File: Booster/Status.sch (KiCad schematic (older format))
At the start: 37 parts

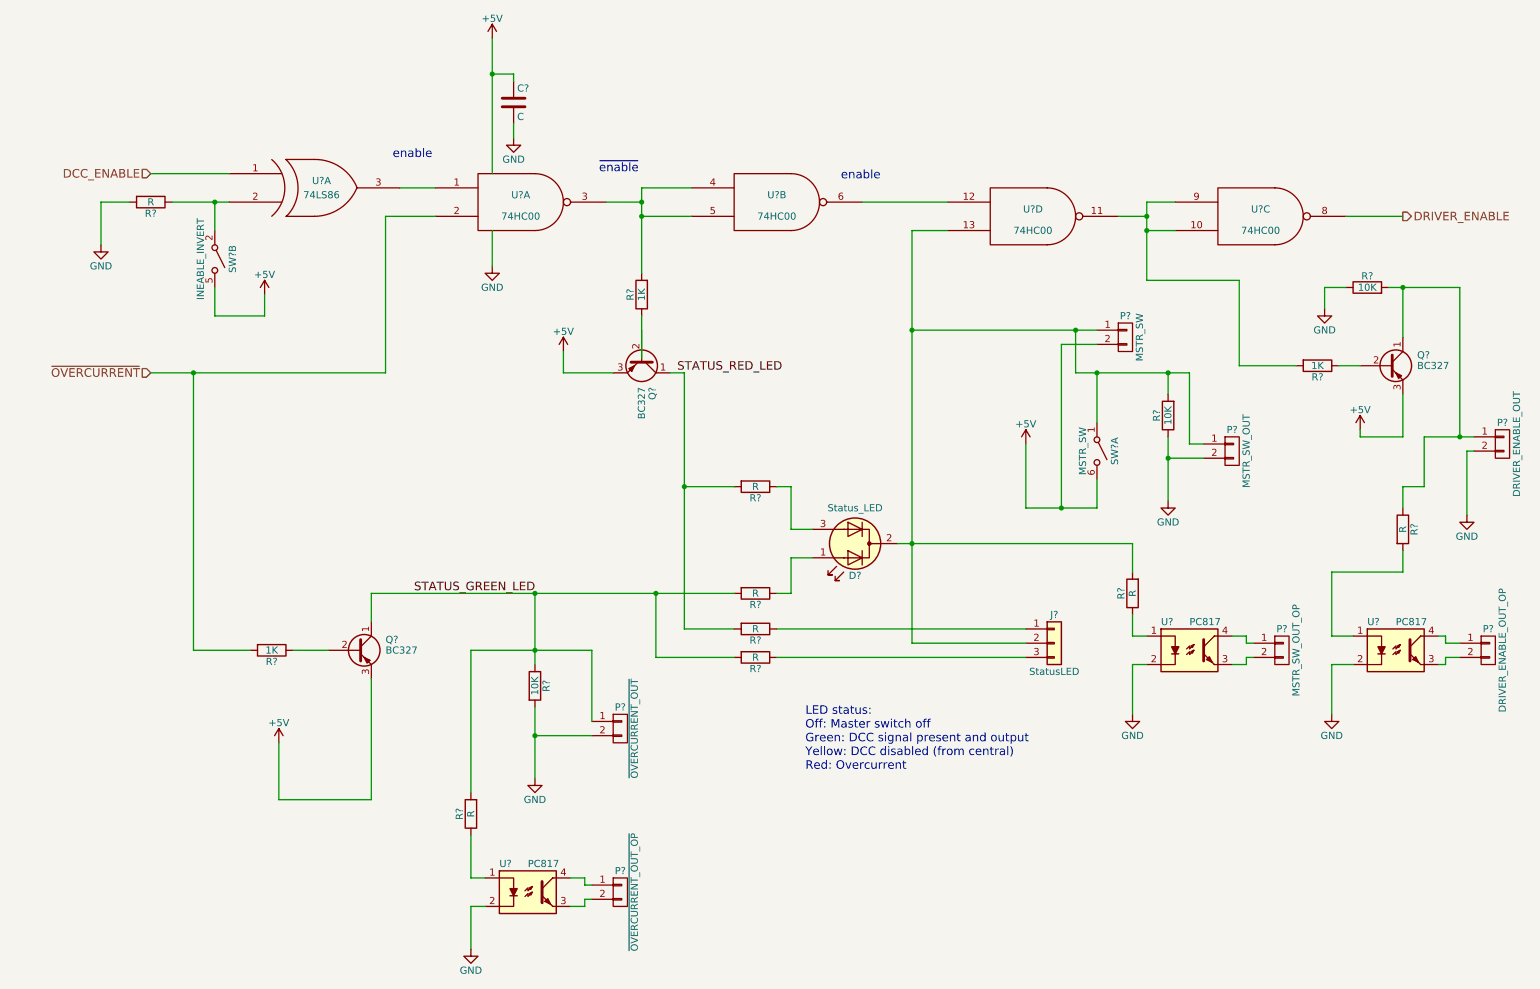
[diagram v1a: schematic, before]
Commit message: Kind of working with the overcurrent retry, but not liking the RC delay in the final output to the motor driver.
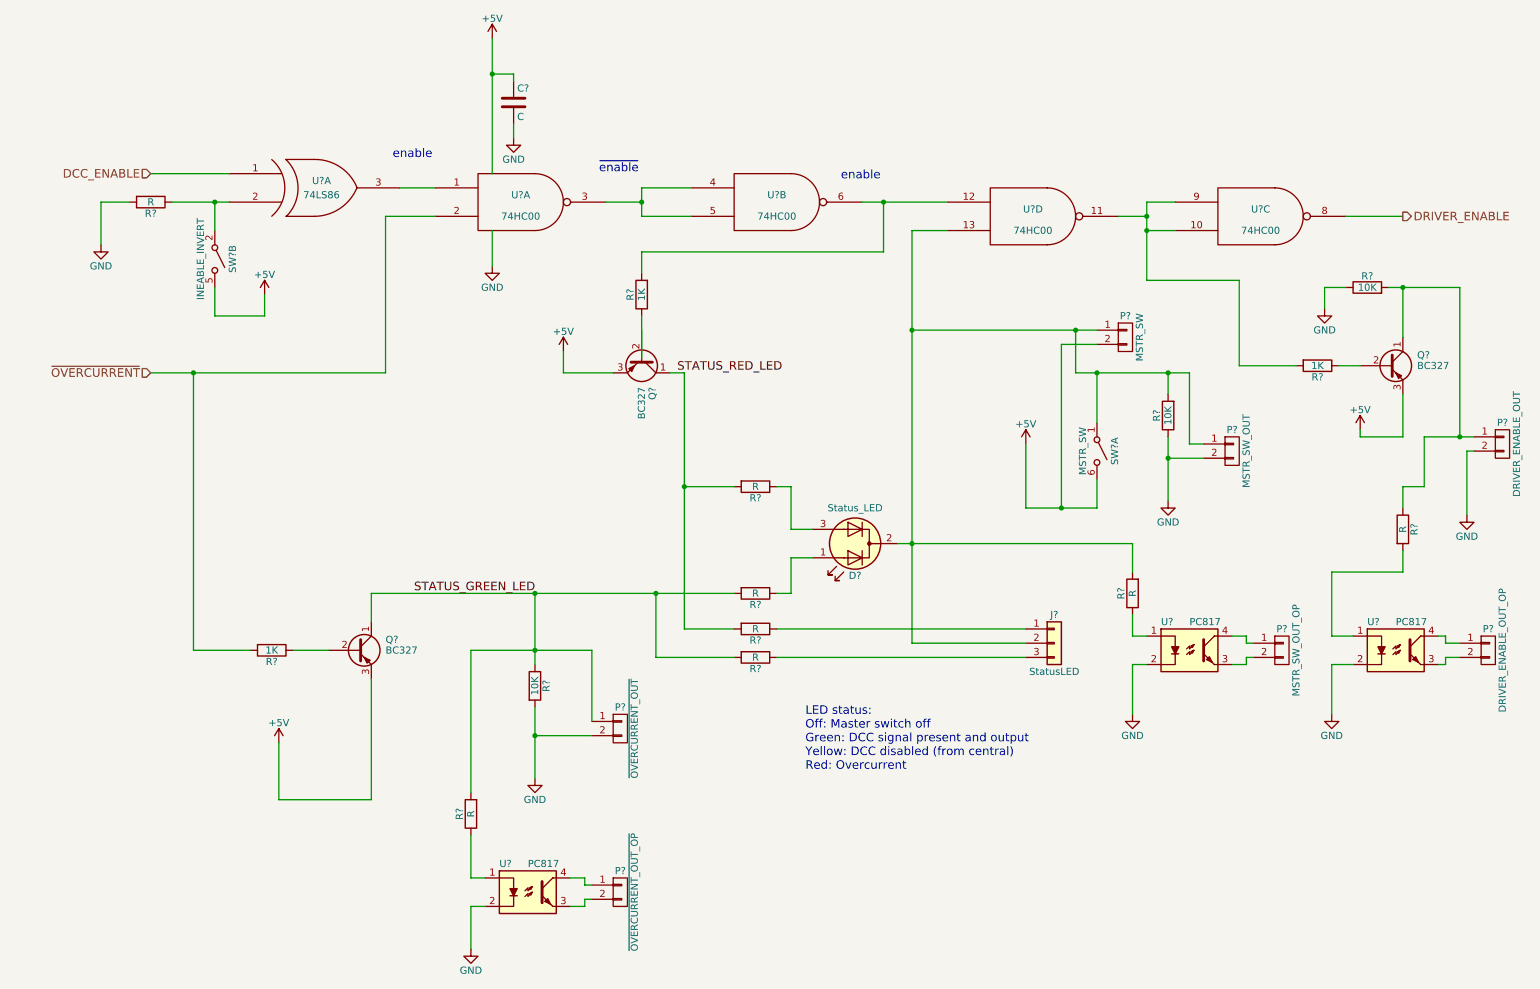
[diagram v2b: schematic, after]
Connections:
- net at U?.3, U?.4, U?.5: no longer R?.2
- net at U?.12, U?.6: now also R?.2
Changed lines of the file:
@@
 $EndComp
 Wire Wire Line
-	1450 3150 1750 3150
-Wire Wire Line
-	1750 3150 3100 3150
+	1450 3150 3100 3150
 Wire Wire Line
 	1450 1750 2000 1750
@@
 	6800 2150 7050 2150
 Wire Wire Line
-	6800 2150 6800 2850
-Wire Wire Line
-	6800 2850 6800 4350
-Wire Wire Line
-	6800 4350 6800 5050
+	6800 2150 6800 5050
 Wire Wire Line
 	7600 4100 7600 3650
@@
 Connection ~ 6800 2850
 Wire Wire Line
-	7600 4100 7850 4100
-Wire Wire Line
-	7850 4100 8100 4100
+	7600 4100 8100 4100
 Wire Wire Line
 	8100 4100 8100 3900
 Wire Wire Line
-	7950 3150 8100 3150
-Wire Wire Line
-	8100 3150 8600 3150
-Wire Wire Line
-	8600 3150 8750 3150
+	7950 3150 8750 3150
 Wire Wire Line
 	7950 3150 7950 2850
@@
 	3000 4900 3000 4700
 Wire Wire Line
-	3000 4700 4150 4700
-Wire Wire Line
-	4150 4700 5000 4700
-Wire Wire Line
-	5000 4700 5550 4700
+	3000 4700 5550 4700
 Wire Wire Line
 	6100 4250 5950 4250
@@
 	5950 4450 6100 4450
 Wire Wire Line
-	5200 3150 5200 3950
-Wire Wire Line
-	5200 3950 5200 4950
+	5200 3150 5200 4950
 Wire Wire Line
 	5200 4950 5550 4950
@@
 Connection ~ 5000 4700
 Wire Wire Line
-	6700 4350 6800 4350
-Wire Wire Line
-	6800 4350 8350 4350
+	6700 4350 8350 4350
 Wire Wire Line
 	6800 5050 7600 5050
@@
 	7850 2950 7850 4100
 Wire Wire Line
-	6800 2850 7950 2850
-Wire Wire Line
-	7950 2850 8100 2850
+	6800 2850 8100 2850
 Connection ~ 7850 4100
 Wire Wire Line
@@
 	10250 2900 10250 2550
 Wire Wire Line
-	10150 2550 10250 2550
-Wire Wire Line
-	10250 2550 10650 2550
+	10150 2550 10650 2550
 Wire Wire Line
 	10650 2550 10650 3600
 Wire Wire Line
-	10400 3600 10650 3600
-Wire Wire Line
-	10650 3600 10750 3600
+	10400 3600 10750 3600
 Wire Wire Line
 	10250 3600 9950 3600
@@
 	9700 2550 9700 2700
 Wire Wire Line
-	4150 4700 4150 5100
-Wire Wire Line
-	4150 5100 4150 5200
+	4150 4700 4150 5200
 Connection ~ 4150 4700
 Wire Wire Line
-	4150 5500 4150 5700
-Wire Wire Line
-	4150 5700 4150 6000
-Wire Wire Line
-	8600 3600 8600 3750
-Wire Wire Line
-	8600 3750 8600 4050
+	4150 5500 4150 6000
+Wire Wire Line
+	8600 3600 8600 4050
 Wire Wire Line
 	8600 3150 8600 3300
@@
 	4550 5100 4550 5600
 Wire Wire Line
-	3700 5100 4150 5100
-Wire Wire Line
-	4150 5100 4550 5100
+	3700 5100 4550 5100
 Connection ~ 4150 5100
 Wire Wire Line
@@
 	4650 1950 4900 1950
 Wire Wire Line
-	4900 1850 4900 1950
-Wire Wire Line
-	4900 1950 4900 2050
-Wire Wire Line
-	4900 2050 4900 2450
-Wire Wire Line
 	4900 1850 5250 1850
 Wire Wire Line
@@
 	8250 2050 8450 2050
 Wire Wire Line
-	8450 1950 8450 2050
-Wire Wire Line
-	8450 2050 8450 2150
-Wire Wire Line
-	8450 2150 8450 2500
+	8450 1950 8450 2500
 Wire Wire Line
 	8450 1950 8650 1950
@@
 Wire Wire Line
 	6450 1950 7050 1950
-Connection ~ 4900 2050
 Wire Wire Line
 	4900 3050 4900 2750
@@
 	9850 2050 10250 2050
 Wire Wire Line
-	1600 1950 1900 1950
-Wire Wire Line
-	1900 1950 2000 1950
+	1600 1950 2000 1950
 Wire Wire Line
 	1300 1950 1100 1950
@@
 	3850 2150 3850 2400
 Wire Wire Line
-	3850 800  3850 1050
-Wire Wire Line
-	3850 1050 3850 1750
+	3850 800  3850 1750
 Wire Wire Line
 	3850 1050 4000 1050
@@
 Wire Wire Line
 	4000 1400 4000 1500
+Wire Wire Line
+	4900 1850 4900 2050
+Wire Wire Line
+	4900 2450 4900 2300
+Wire Wire Line
+	4900 2300 6600 2300
+Wire Wire Line
+	6600 2300 6600 1950
+Connection ~ 6600 1950
 $EndSCHEMATC

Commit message: Added 555 timer to control overcurrent release delay. Simpler to control as turning the power off cleared the overflow before the capacitor controlling the release delay was fully cleared. The LM339 is still doing the detect delay.
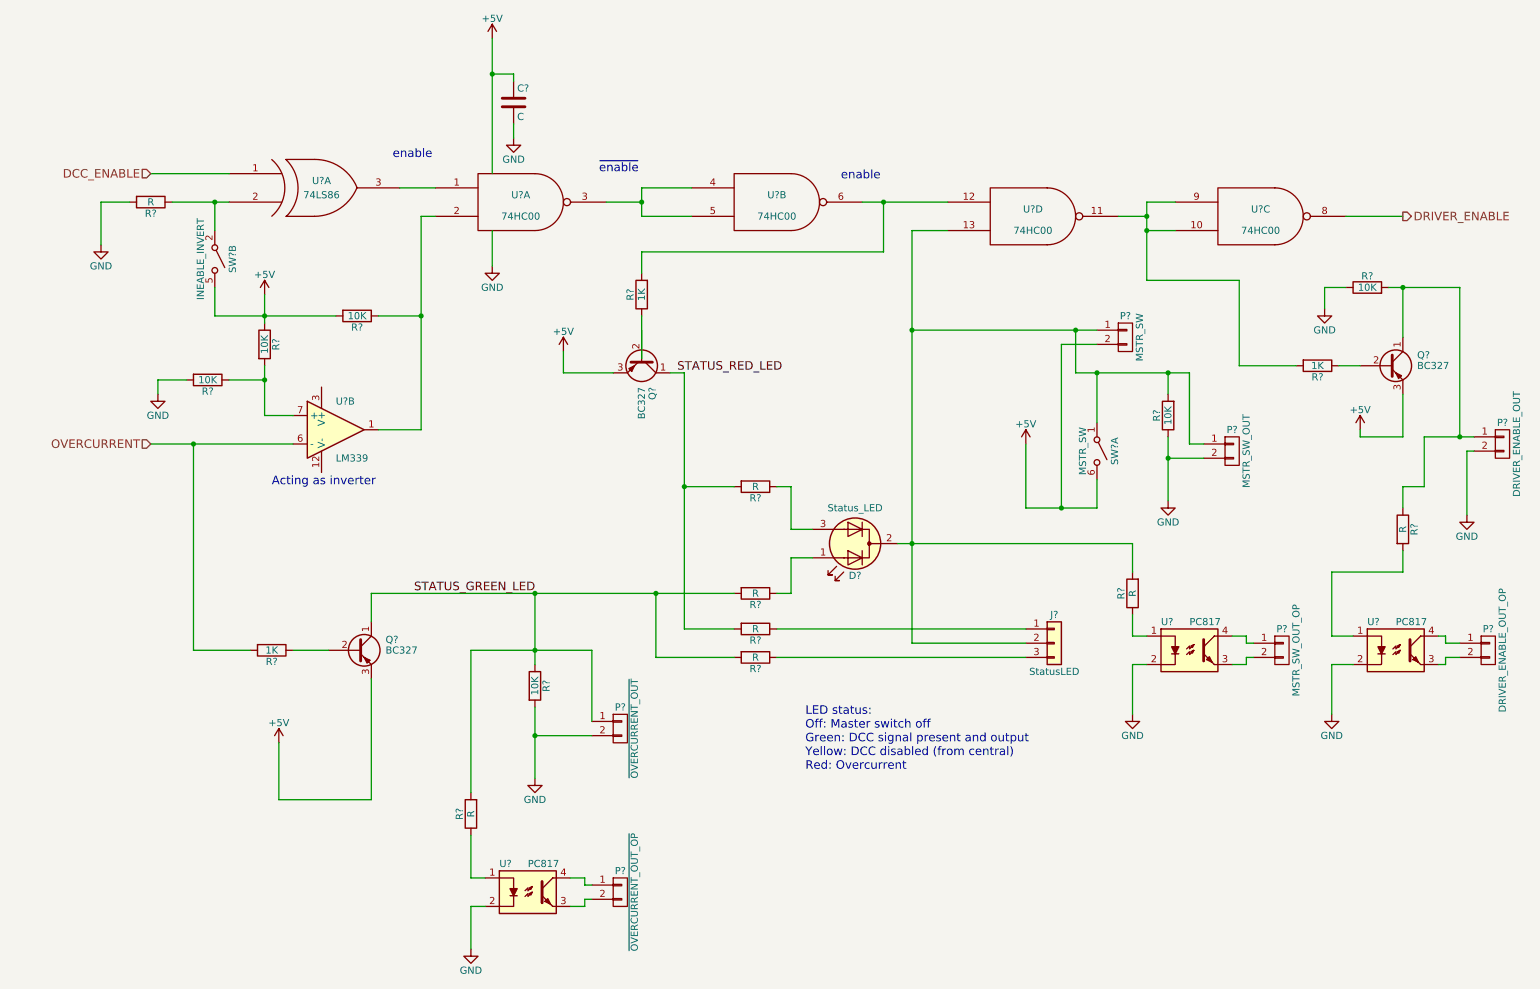
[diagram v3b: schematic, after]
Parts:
- added R? (x3): 10K, symbol R
- added U?: LM339, symbol LM339
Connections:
- net +5V: now also R?.1, R?.2
- net GND: now also R?.2
- net ~OVERCURRENT: no longer names the net of U?.2
- net ~OVERCURRENT: now also R?.1, U?.1; no longer R?.2
- new net: R?.1, R?.2, U?.7 (+)
- new net OVERCURRENT: R?.2, U?.6 (-)
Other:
- note added: "Acting as inverter"
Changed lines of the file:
@@
 Text HLabel 1450 1750 0    60   Input ~ 0
 DCC_ENABLE
-Text HLabel 1450 3150 0    60   Input ~ 0
-~OVERCURRENT
+Text HLabel 1450 3650 0    60   Input ~ 0
+OVERCURRENT
 Text HLabel 10250 2050 2    60   Output ~ 0
 DRIVER_ENABLE
@@
 $EndComp
 Wire Wire Line
-	1450 3150 3100 3150
-Wire Wire Line
 	1450 1750 2000 1750
 Wire Wire Line
-	1750 3150 1750 5100
+	1750 3650 1750 5100
 Wire Wire Line
 	6800 2150 7050 2150
 Wire Wire Line
-	6800 2150 6800 5050
+	6800 2150 6800 2850
+Wire Wire Line
+	6800 2850 6800 4350
+Wire Wire Line
+	6800 4350 6800 5050
 Wire Wire Line
 	7600 4100 7600 3650
@@
 Connection ~ 6800 2850
 Wire Wire Line
-	7600 4100 8100 4100
+	7600 4100 7850 4100
+Wire Wire Line
+	7850 4100 8100 4100
 Wire Wire Line
 	8100 4100 8100 3900
 Wire Wire Line
-	7950 3150 8750 3150
+	7950 3150 8100 3150
+Wire Wire Line
+	8100 3150 8600 3150
+Wire Wire Line
+	8600 3150 8750 3150
 Wire Wire Line
 	7950 3150 7950 2850
@@
 Wire Wire Line
 	1750 5100 2150 5100
-Connection ~ 1750 3150
+Connection ~ 1750 3650
 Wire Wire Line
 	2450 5100 2700 5100
@@
 	3000 4900 3000 4700
 Wire Wire Line
-	3000 4700 5550 4700
+	3000 4700 4150 4700
+Wire Wire Line
+	4150 4700 5000 4700
+Wire Wire Line
+	5000 4700 5550 4700
 Wire Wire Line
 	6100 4250 5950 4250
@@
 	5950 4450 6100 4450
 Wire Wire Line
-	5200 3150 5200 4950
+	5200 3150 5200 3950
+Wire Wire Line
+	5200 3950 5200 4950
 Wire Wire Line
 	5200 4950 5550 4950
@@
 Connection ~ 5000 4700
 Wire Wire Line
-	6700 4350 8350 4350
+	6700 4350 6800 4350
+Wire Wire Line
+	6800 4350 8350 4350
 Wire Wire Line
 	6800 5050 7600 5050
@@
 	7850 2950 7850 4100
 Wire Wire Line
-	6800 2850 8100 2850
+	6800 2850 7950 2850
+Wire Wire Line
+	7950 2850 8100 2850
 Connection ~ 7850 4100
 Wire Wire Line
@@
 	10250 2900 10250 2550
 Wire Wire Line
-	10150 2550 10650 2550
+	10150 2550 10250 2550
+Wire Wire Line
+	10250 2550 10650 2550
 Wire Wire Line
 	10650 2550 10650 3600
 Wire Wire Line
-	10400 3600 10750 3600
+	10400 3600 10650 3600
+Wire Wire Line
+	10650 3600 10750 3600
 Wire Wire Line
 	10250 3600 9950 3600
@@
 	9700 2550 9700 2700
 Wire Wire Line
-	4150 4700 4150 5200
+	4150 4700 4150 5100
+Wire Wire Line
+	4150 5100 4150 5200
 Connection ~ 4150 4700
 Wire Wire Line
-	4150 5500 4150 6000
-Wire Wire Line
-	8600 3600 8600 4050
+	4150 5500 4150 5700
+Wire Wire Line
+	4150 5700 4150 6000
+Wire Wire Line
+	8600 3600 8600 3750
+Wire Wire Line
+	8600 3750 8600 4050
 Wire Wire Line
 	8600 3150 8600 3300
@@
 	4550 5100 4550 5600
 Wire Wire Line
-	3700 5100 4550 5100
+	3700 5100 4150 5100
+Wire Wire Line
+	4150 5100 4550 5100
 Connection ~ 4150 5100
 Wire Wire Line
@@
 	3700 6900 3700 7200
 Wire Wire Line
-	3100 3150 3100 2050
-Wire Wire Line
-	3100 2050 3450 2050
+	3350 2050 3350 2750
+Wire Wire Line
+	3350 2750 3350 3550
+Wire Wire Line
+	3350 2050 3450 2050
 Wire Wire Line
 	3200 1850 3450 1850
@@
 	8250 2050 8450 2050
 Wire Wire Line
-	8450 1950 8450 2500
+	8450 1950 8450 2050
+Wire Wire Line
+	8450 2050 8450 2150
+Wire Wire Line
+	8450 2150 8450 2500
 Wire Wire Line
 	8450 1950 8650 1950
@@
 Connection ~ 8450 2150
 Wire Wire Line
-	6450 1950 7050 1950
+	6450 1950 6600 1950
+Wire Wire Line
+	6600 1950 7050 1950
 Wire Wire Line
 	4900 3050 4900 2750
@@
 	9850 2050 10250 2050
 Wire Wire Line
-	1600 1950 2000 1950
+	1600 1950 1900 1950
+Wire Wire Line
+	1900 1950 2000 1950
 Wire Wire Line
 	1300 1950 1100 1950
@@
 	1900 2750 2250 2750
 Wire Wire Line
-	2250 2750 2250 2600
+	2250 2750 2750 2750
+Wire Wire Line
+	2250 2600 2250 2750
+Wire Wire Line
+	2250 2750 2250 2800
 Wire Wire Line
 	3850 2150 3850 2400
 Wire Wire Line
-	3850 800  3850 1750
+	3850 800  3850 1050
+Wire Wire Line
+	3850 1050 3850 1750
 Wire Wire Line
 	3850 1050 4000 1050
@@
 	4000 1400 4000 1500
 Wire Wire Line
-	4900 1850 4900 2050
+	4900 1850 4900 1950
+Wire Wire Line
+	4900 1950 4900 2050
 Wire Wire Line
 	4900 2450 4900 2300
@@
 	6600 2300 6600 1950
 Connection ~ 6600 1950
+$Comp
+L LM339 U?
+U 2 1 5A375C9A
+P 2750 3550
+F 0 "U?" H 2750 3750 50  0000 L CNN
+F 1 "LM339" H 2750 3350 50  0000 L CNN
+F 2 "" H 2700 3650 50  0000 C CNN
+F 3 "" H 2800 3750 50  0000 C CNN
+	2    2750 3550
+	1    0    0    -1
+$EndComp
+Wire Wire Line
+	1450 3650 1750 3650
+Wire Wire Line
+	1750 3650 2450 3650
+Wire Wire Line
+	2250 3450 2450 3450
+Wire Wire Line
+	2250 3100 2250 3200
+Wire Wire Line
+	2250 3200 2250 3450
+Wire Wire Line
+	2000 3200 2250 3200
+$Comp
+L R R?
+U 1 1 5A376953
+P 2250 2950
+F 0 "R?" V 2330 2950 50  0000 C CNN
+F 1 "10K" V 2250 2950 50  0000 C CNN
+F 2 "" V 2180 2950 50  0000 C CNN
+F 3 "" H 2250 2950 50  0000 C CNN
+	1    2250 2950
+	1    0    0    -1
+$EndComp
+Connection ~ 2250 3200
+Connection ~ 2250 2750
+$Comp
+L R R?
+U 1 1 5A376D88
+P 1850 3200
+F 0 "R?" V 1930 3200 50  0000 C CNN
+F 1 "10K" V 1850 3200 50  0000 C CNN
+F 2 "" V 1780 3200 50  0000 C CNN
+F 3 "" H 1850 3200 50  0000 C CNN
+	1    1850 3200
+	0    1    1    0
+$EndComp
+Wire Wire Line
+	1700 3200 1500 3200
+Wire Wire Line
+	1500 3200 1500 3300
+$Comp
+L GND #PWR?
+U 1 1 5A376ECE
+P 1500 3300
+F 0 "#PWR?" H 1500 3050 50  0001 C CNN
+F 1 "GND" H 1500 3150 50  0000 C CNN
+F 2 "" H 1500 3300 50  0000 C CNN
+F 3 "" H 1500 3300 50  0000 C CNN
+	1    1500 3300
+	1    0    0    -1
+$EndComp
+Wire Wire Line
+	3350 3550 3050 3550
+$Comp
+L R R?
+U 1 1 5A377144
+P 2900 2750
+F 0 "R?" V 2980 2750 50  0000 C CNN
+F 1 "10K" V 2900 2750 50  0000 C CNN
+F 2 "" V 2830 2750 50  0000 C CNN
+F 3 "" H 2900 2750 50  0000 C CNN
+	1    2900 2750
+	0    1    1    0
+$EndComp
+Wire Wire Line
+	3050 2750 3350 2750
+Connection ~ 3350 2750
+Text Notes 2300 3950 0    60   ~ 0
+Acting as inverter
 $EndSCHEMATC

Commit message: Hooking up reset of overcurrent to DCC Enable. Most likely going to change it to the master switch instead (detecting both would be nice, but probably not worth introducing yet another IC for).
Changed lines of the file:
@@
 	6800 2150 7050 2150
 Wire Wire Line
-	6800 2150 6800 2850
-Wire Wire Line
-	6800 2850 6800 4350
-Wire Wire Line
-	6800 4350 6800 5050
+	6800 2150 6800 5050
 Wire Wire Line
 	7600 4100 7600 3650
@@
 Connection ~ 6800 2850
 Wire Wire Line
-	7600 4100 7850 4100
-Wire Wire Line
-	7850 4100 8100 4100
+	7600 4100 8100 4100
 Wire Wire Line
 	8100 4100 8100 3900
 Wire Wire Line
-	7950 3150 8100 3150
-Wire Wire Line
-	8100 3150 8600 3150
-Wire Wire Line
-	8600 3150 8750 3150
+	7950 3150 8750 3150
 Wire Wire Line
 	7950 3150 7950 2850
@@
 	3000 4900 3000 4700
 Wire Wire Line
-	3000 4700 4150 4700
-Wire Wire Line
-	4150 4700 5000 4700
-Wire Wire Line
-	5000 4700 5550 4700
+	3000 4700 5550 4700
 Wire Wire Line
 	6100 4250 5950 4250
@@
 	5950 4450 6100 4450
 Wire Wire Line
-	5200 3150 5200 3950
-Wire Wire Line
-	5200 3950 5200 4950
+	5200 3150 5200 4950
 Wire Wire Line
 	5200 4950 5550 4950
@@
 Connection ~ 5000 4700
 Wire Wire Line
-	6700 4350 6800 4350
-Wire Wire Line
-	6800 4350 8350 4350
+	6700 4350 8350 4350
 Wire Wire Line
 	6800 5050 7600 5050
@@
 	7850 2950 7850 4100
 Wire Wire Line
-	6800 2850 7950 2850
-Wire Wire Line
-	7950 2850 8100 2850
+	6800 2850 8100 2850
 Connection ~ 7850 4100
 Wire Wire Line
@@
 	10250 2900 10250 2550
 Wire Wire Line
-	10150 2550 10250 2550
-Wire Wire Line
-	10250 2550 10650 2550
+	10150 2550 10650 2550
 Wire Wire Line
 	10650 2550 10650 3600
 Wire Wire Line
-	10400 3600 10650 3600
-Wire Wire Line
-	10650 3600 10750 3600
+	10400 3600 10750 3600
 Wire Wire Line
 	10250 3600 9950 3600
@@
 	9700 2550 9700 2700
 Wire Wire Line
-	4150 4700 4150 5100
-Wire Wire Line
-	4150 5100 4150 5200
+	4150 4700 4150 5200
 Connection ~ 4150 4700
 Wire Wire Line
-	4150 5500 4150 5700
-Wire Wire Line
-	4150 5700 4150 6000
-Wire Wire Line
-	8600 3600 8600 3750
-Wire Wire Line
-	8600 3750 8600 4050
+	4150 5500 4150 6000
+Wire Wire Line
+	8600 3600 8600 4050
 Wire Wire Line
 	8600 3150 8600 3300
@@
 	4550 5100 4550 5600
 Wire Wire Line
-	3700 5100 4150 5100
-Wire Wire Line
-	4150 5100 4550 5100
+	3700 5100 4550 5100
 Connection ~ 4150 5100
 Wire Wire Line
@@
 	3700 6900 3700 7200
 Wire Wire Line
-	3350 2050 3350 2750
-Wire Wire Line
-	3350 2750 3350 3550
+	3350 2050 3350 3550
 Wire Wire Line
 	3350 2050 3450 2050
@@
 	8250 2050 8450 2050
 Wire Wire Line
-	8450 1950 8450 2050
-Wire Wire Line
-	8450 2050 8450 2150
-Wire Wire Line
-	8450 2150 8450 2500
+	8450 1950 8450 2500
 Wire Wire Line
 	8450 1950 8650 1950
@@
 Connection ~ 8450 2150
 Wire Wire Line
-	6450 1950 6600 1950
-Wire Wire Line
-	6600 1950 7050 1950
+	6450 1950 7050 1950
 Wire Wire Line
 	4900 3050 4900 2750
@@
 	9850 2050 10250 2050
 Wire Wire Line
-	1600 1950 1900 1950
-Wire Wire Line
-	1900 1950 2000 1950
+	1600 1950 2000 1950
 Wire Wire Line
 	1300 1950 1100 1950
@@
 	1900 2550 1900 2750
 Wire Wire Line
-	1900 2750 2250 2750
-Wire Wire Line
-	2250 2750 2750 2750
-Wire Wire Line
-	2250 2600 2250 2750
-Wire Wire Line
-	2250 2750 2250 2800
+	1900 2750 2750 2750
+Wire Wire Line
+	2250 2600 2250 2800
 Wire Wire Line
 	3850 2150 3850 2400
 Wire Wire Line
-	3850 800  3850 1050
-Wire Wire Line
-	3850 1050 3850 1750
+	3850 800  3850 1750
 Wire Wire Line
 	3850 1050 4000 1050
@@
 	4000 1400 4000 1500
 Wire Wire Line
-	4900 1850 4900 1950
-Wire Wire Line
-	4900 1950 4900 2050
+	4900 1850 4900 2050
 Wire Wire Line
 	4900 2450 4900 2300
@@
 $EndComp
 Wire Wire Line
-	1450 3650 1750 3650
-Wire Wire Line
-	1750 3650 2450 3650
+	1450 3650 2450 3650
 Wire Wire Line
 	2250 3450 2450 3450
 Wire Wire Line
-	2250 3100 2250 3200
-Wire Wire Line
-	2250 3200 2250 3450
+	2250 3100 2250 3450
 Wire Wire Line
 	2000 3200 2250 3200
